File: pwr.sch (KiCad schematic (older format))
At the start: 60 parts, among them U1 FT601, U10 MIC94310, U11 PAM2305, U4 ECP5, U6 PAM2305, U7 NCP186, U8 MIC94310, U9 MIC94310, X2 CONN_01X08

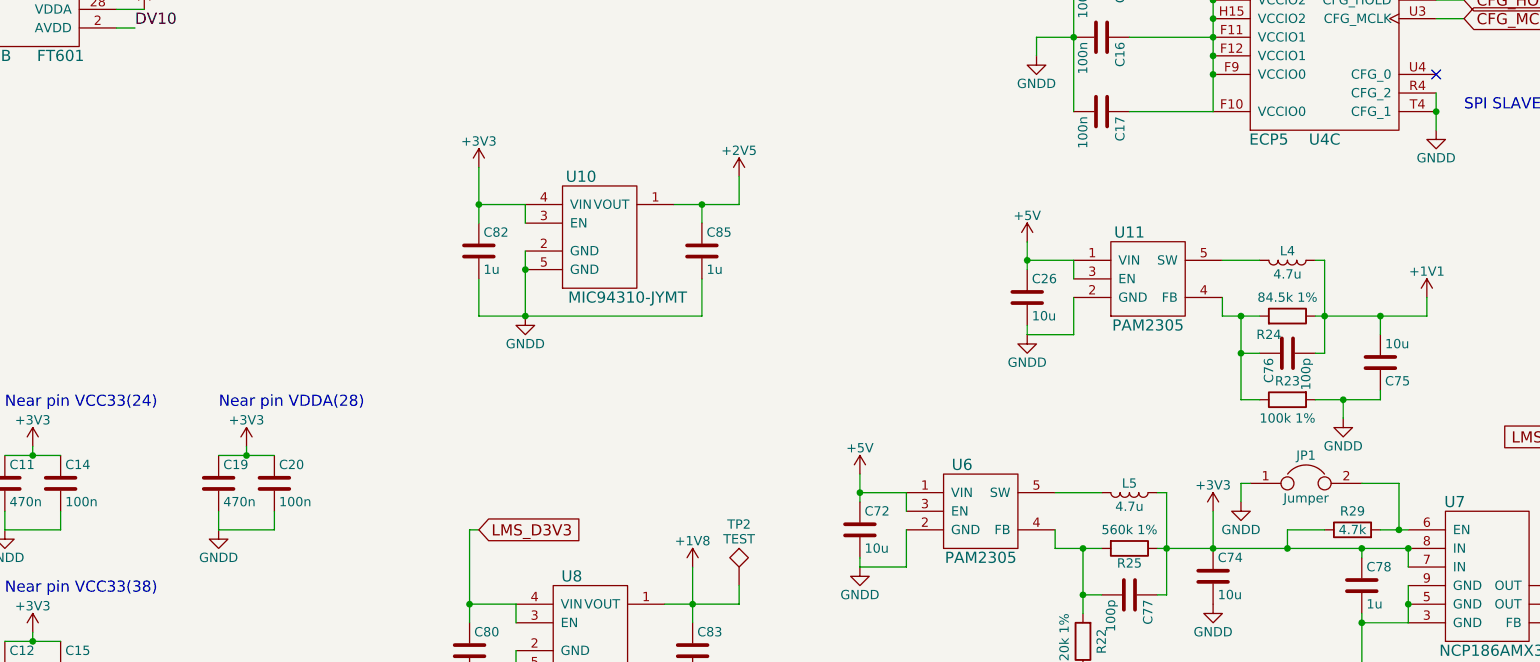
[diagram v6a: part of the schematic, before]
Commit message: Add leds. Traced LMS_3V3A LDO.
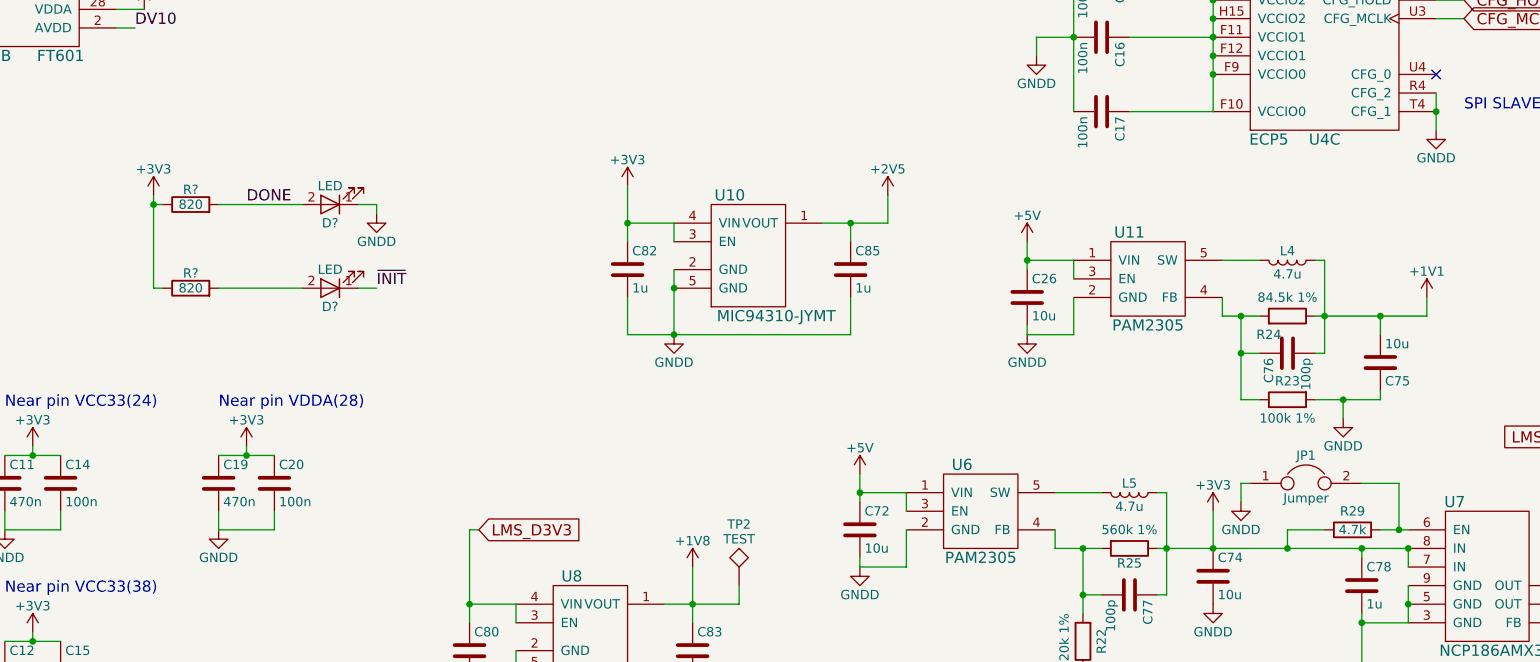
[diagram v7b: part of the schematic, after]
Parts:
- added D? (x2): LED, symbol LED
- added R? (x2): 820, symbol R
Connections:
- net +3V3: now also R?.1, R?.1
- net DONE: now also D?.2 (A), R?.2
- net GNDD: now also D?.1 (K)
- net ~INIT: now also D?.1 (K)
- new net: D?.2 (A), R?.2
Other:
- moved on the sheet: C82, C85, U10
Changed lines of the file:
@@
 	3950 7100 3950 7450
 $Comp
-L GNDD #PWR026
+L GNDD #PWR025
 U 1 1 58A7B03F
 P 3950 7450
-F 0 "#PWR026" H 3950 7200 50  0001 C CNN
+F 0 "#PWR025" H 3950 7200 50  0001 C CNN
 F 1 "GNDD" H 3950 7300 50  0000 C CNN
 F 2 "" H 3950 7450 50  0000 C CNN
@@
 Connection ~ 3950 7450
 $Comp
-L +1V8 #PWR027
+L +1V8 #PWR026
 U 1 1 58A7B123
 P 5850 5300
-F 0 "#PWR027" H 5850 5150 50  0001 C CNN
+F 0 "#PWR026" H 5850 5150 50  0001 C CNN
 F 1 "+1V8" H 5850 5440 50  0000 C CNN
 F 2 "" H 5850 5300 50  0000 C CNN
@@
 L MIC94310 U10
 U 1 1 58A7CAA3
-P 5150 3800
-F 0 "U10" H 5250 4400 60  0000 C CNN
-F 1 "MIC94310" H 5350 3750 60  0001 C CNN
-F 2 "sdr-foots:DFN-4" H 4600 3650 60  0001 C CNN
-F 3 "" H 4600 3650 60  0001 C CNN
-F 4 "MIC94310-JYMT" H 5500 3750 60  0000 C CNN "Part"
-	1    5150 3800
+P 5950 3900
+F 0 "U10" H 6050 4500 60  0000 C CNN
+F 1 "MIC94310" H 6150 3850 60  0001 C CNN
+F 2 "sdr-foots:DFN-4" H 5400 3750 60  0001 C CNN
+F 3 "" H 5400 3750 60  0001 C CNN
+F 4 "MIC94310-JYMT" H 6300 3850 60  0000 C CNN "Part"
+	1    5950 3900
 	1    0    0    -1
 $EndComp
@@
 L C C85
 U 1 1 58A7CAA9
-P 5900 3600
-F 0 "C85" H 5925 3700 50  0000 L CNN
-F 1 "1u" H 5925 3500 50  0000 L CNN
-F 2 "Capacitors_SMD:C_0603" H 5938 3450 50  0001 C CNN
-F 3 "" H 5900 3600 50  0000 C CNN
-	1    5900 3600
-	1    0    0    -1
-$EndComp
-Wire Wire Line
-	4950 3450 4950 3350
-Wire Wire Line
-	4950 3600 4950 3950
-$Comp
-L GNDD #PWR028
+P 6700 3700
+F 0 "C85" H 6725 3800 50  0000 L CNN
+F 1 "1u" H 6725 3600 50  0000 L CNN
+F 2 "Capacitors_SMD:C_0603" H 6738 3550 50  0001 C CNN
+F 3 "" H 6700 3700 50  0000 C CNN
+	1    6700 3700
+	1    0    0    -1
+$EndComp
+Wire Wire Line
+	5750 3550 5750 3450
+Wire Wire Line
+	5750 3700 5750 4050
+$Comp
+L GNDD #PWR027
 U 1 1 58A7CAB1
-P 4950 3950
-F 0 "#PWR028" H 4950 3700 50  0001 C CNN
-F 1 "GNDD" H 4950 3800 50  0000 C CNN
-F 2 "" H 4950 3950 50  0000 C CNN
-F 3 "" H 4950 3950 50  0000 C CNN
-	1    4950 3950
-	1    0    0    -1
-$EndComp
-Connection ~ 4950 3700
-Wire Wire Line
-	5900 3950 5900 3750
-Wire Wire Line
-	4700 3950 5900 3950
-Wire Wire Line
-	5900 3450 5900 3350
-Wire Wire Line
-	5750 3350 6100 3350
+P 5750 4050
+F 0 "#PWR027" H 5750 3800 50  0001 C CNN
+F 1 "GNDD" H 5750 3900 50  0000 C CNN
+F 2 "" H 5750 4050 50  0000 C CNN
+F 3 "" H 5750 4050 50  0000 C CNN
+	1    5750 4050
+	1    0    0    -1
+$EndComp
+Connection ~ 5750 3800
+Wire Wire Line
+	6700 4050 6700 3850
+Wire Wire Line
+	5500 4050 6700 4050
+Wire Wire Line
+	6700 3550 6700 3450
+Wire Wire Line
+	6550 3450 6900 3450
 $Comp
 L C C82
 U 1 1 58A7CABC
-P 4700 3600
-F 0 "C82" H 4725 3700 50  0000 L CNN
-F 1 "1u" H 4725 3500 50  0000 L CNN
-F 2 "Capacitors_SMD:C_0603" H 4738 3450 50  0001 C CNN
-F 3 "" H 4700 3600 50  0000 C CNN
-	1    4700 3600
-	1    0    0    -1
-$EndComp
-Wire Wire Line
-	4700 3150 4700 3450
-Wire Wire Line
-	4950 3350 4700 3350
-Wire Wire Line
-	4700 3750 4700 3950
-Connection ~ 4950 3950
-$Comp
-L +3V3 #PWR029
+P 5500 3700
+F 0 "C82" H 5525 3800 50  0000 L CNN
+F 1 "1u" H 5525 3600 50  0000 L CNN
+F 2 "Capacitors_SMD:C_0603" H 5538 3550 50  0001 C CNN
+F 3 "" H 5500 3700 50  0000 C CNN
+	1    5500 3700
+	1    0    0    -1
+$EndComp
+Wire Wire Line
+	5500 3250 5500 3550
+Wire Wire Line
+	5750 3450 5500 3450
+Wire Wire Line
+	5500 3850 5500 4050
+Connection ~ 5750 4050
+$Comp
+L +3V3 #PWR028
 U 1 1 58A7CAC6
-P 4700 3150
-F 0 "#PWR029" H 4700 3000 50  0001 C CNN
-F 1 "+3V3" H 4700 3290 50  0000 C CNN
-F 2 "" H 4700 3150 50  0000 C CNN
-F 3 "" H 4700 3150 50  0000 C CNN
-	1    4700 3150
-	1    0    0    -1
-$EndComp
-Connection ~ 4700 3350
-Connection ~ 5900 3350
+P 5500 3250
+F 0 "#PWR028" H 5500 3100 50  0001 C CNN
+F 1 "+3V3" H 5500 3390 50  0000 C CNN
+F 2 "" H 5500 3250 50  0000 C CNN
+F 3 "" H 5500 3250 50  0000 C CNN
+	1    5500 3250
+	1    0    0    -1
+$EndComp
+Connection ~ 5500 3450
+Connection ~ 6700 3450
 Wire Wire Line
 	9850 1500 9900 1500
@@
 Connection ~ 8650 1050
 $Comp
-L +3V3 #PWR030
+L +3V3 #PWR029
 U 1 1 58AD72E7
 P 8400 1250
-F 0 "#PWR030" H 8400 1100 50  0001 C CNN
+F 0 "#PWR029" H 8400 1100 50  0001 C CNN
 F 1 "+3V3" H 8400 1390 50  0000 C CNN
 F 2 "" H 8400 1250 50  0000 C CNN
@@
 Connection ~ 7900 1250
 $Comp
-L GNDD #PWR031
+L GNDD #PWR030
 U 1 1 58AD91E3
 P 7700 2550
-F 0 "#PWR031" H 7700 2300 50  0001 C CNN
+F 0 "#PWR030" H 7700 2300 50  0001 C CNN
 F 1 "GNDD" H 7700 2400 50  0000 C CNN
 F 2 "" H 7700 2550 50  0000 C CNN
@@
 $EndComp
 $Comp
-L +3V3 #PWR032
+L +3V3 #PWR031
 U 1 1 58AEBAC7
 P 6400 950
-F 0 "#PWR032" H 6400 800 50  0001 C CNN
+F 0 "#PWR031" H 6400 800 50  0001 C CNN
 F 1 "+3V3" H 6400 1090 50  0000 C CNN
 F 2 "" H 6400 950 50  0000 C CNN
@@
 $EndComp
 $Comp
-L GNDD #PWR033
+L GNDD #PWR032
 U 1 1 58B9309E
 P 7650 4050
-F 0 "#PWR033" H 7650 3800 50  0001 C CNN
+F 0 "#PWR032" H 7650 3800 50  0001 C CNN
 F 1 "GNDD" H 7650 3900 50  0000 C CNN
 F 2 "" H 7650 4050 50  0000 C CNN
@@
 	7650 4050 7650 4000
 $Comp
-L +5V #PWR034
+L +5V #PWR033
 U 1 1 58B930A5
 P 7650 3550
-F 0 "#PWR034" H 7650 3400 50  0001 C CNN
+F 0 "#PWR033" H 7650 3400 50  0001 C CNN
 F 1 "+5V" H 7650 3690 50  0000 C CNN
 F 2 "" H 7650 3550 50  0000 C CNN
@@
 Connection ~ 8650 1550
 $Comp
-L +2V5 #PWR035
+L +2V5 #PWR034
 U 1 1 58BCAEE2
-P 6100 3200
-F 0 "#PWR035" H 6100 3050 50  0001 C CNN
-F 1 "+2V5" H 6100 3340 50  0000 C CNN
-F 2 "" H 6100 3200 50  0000 C CNN
-F 3 "" H 6100 3200 50  0000 C CNN
-	1    6100 3200
-	1    0    0    -1
-$EndComp
-Wire Wire Line
-	6100 3350 6100 3200
+P 6900 3300
+F 0 "#PWR034" H 6900 3150 50  0001 C CNN
+F 1 "+2V5" H 6900 3440 50  0000 C CNN
+F 2 "" H 6900 3300 50  0000 C CNN
+F 3 "" H 6900 3300 50  0000 C CNN
+	1    6900 3300
+	1    0    0    -1
+$EndComp
+Wire Wire Line
+	6900 3450 6900 3300
 $Comp
 L Ferrite_Bead L3
@@
 	8200 950  8650 950
 $Comp
-L GNDD #PWR036
+L GNDD #PWR035
 U 1 1 58D24E6E
 P 9450 5900
-F 0 "#PWR036" H 9450 5650 50  0001 C CNN
+F 0 "#PWR035" H 9450 5650 50  0001 C CNN
 F 1 "GNDD" H 9450 5750 50  0000 C CNN
 F 2 "" H 9450 5900 50  0000 C CNN
@@
 	6100 5500 6100 5400
 Wire Wire Line
-	9700 5100 9550 5100
+	9550 5100 9700 5100
 Wire Wire Line
 	9450 4850 9650 4850
@@
 Connection ~ 9650 5100
 $Comp
-L GNDD #PWR037
+L GNDD #PWR036
 U 1 1 5936655F
 P 8800 4950
-F 0 "#PWR037" H 8800 4700 50  0001 C CNN
+F 0 "#PWR036" H 8800 4700 50  0001 C CNN
 F 1 "GNDD" H 8800 4800 50  0000 C CNN
 F 2 "" H 8800 4950 50  0000 C CNN
@@
 Wire Wire Line
 	4650 5100 4700 5100
+$Comp
+L R R?
+U 1 1 593912E7
+P 3150 3350
+F 0 "R?" V 3230 3350 50  0000 C CNN
+F 1 "820" V 3150 3350 50  0000 C CNN
+F 2 "" V 3080 3350 50  0001 C CNN
+F 3 "" H 3150 3350 50  0001 C CNN
+	1    3150 3350
+	0    -1   -1   0
+$EndComp
+$Comp
+L R R?
+U 1 1 593913B6
+P 3150 3800
+F 0 "R?" V 3230 3800 50  0000 C CNN
+F 1 "820" V 3150 3800 50  0000 C CNN
+F 2 "" V 3080 3800 50  0001 C CNN
+F 3 "" H 3150 3800 50  0001 C CNN
+	1    3150 3800
+	0    -1   -1   0
+$EndComp
+$Comp
+L LED D?
+U 1 1 5939158A
+P 3900 3350
+F 0 "D?" H 3900 3450 50  0000 C CNN
+F 1 "LED" H 3900 3250 50  0000 C CNN
+F 2 "" H 3900 3350 50  0001 C CNN
+F 3 "" H 3900 3350 50  0001 C CNN
+	1    3900 3350
+	-1   0    0    1
+$EndComp
+$Comp
+L LED D?
+U 1 1 5939162D
+P 3900 3800
+F 0 "D?" H 3900 3900 50  0000 C CNN
+F 1 "LED" H 3900 3700 50  0000 C CNN
+F 2 "" H 3900 3800 50  0001 C CNN
+F 3 "" H 3900 3800 50  0001 C CNN
+	1    3900 3800
+	-1   0    0    1
+$EndComp
+$Comp
+L +3V3 #PWR?
+U 1 1 593919B2
+P 2950 3300
+F 0 "#PWR?" H 2950 3150 50  0001 C CNN
+F 1 "+3V3" H 2950 3440 50  0000 C CNN
+F 2 "" H 2950 3300 50  0000 C CNN
+F 3 "" H 2950 3300 50  0000 C CNN
+	1    2950 3300
+	1    0    0    -1
+$EndComp
+Wire Wire Line
+	3300 3350 3750 3350
+Wire Wire Line
+	2950 3350 3000 3350
+Wire Wire Line
+	2950 3800 3000 3800
+Wire Wire Line
+	2950 3300 2950 3800
+Connection ~ 2950 3350
+Wire Wire Line
+	3300 3800 3750 3800
+$Comp
+L GNDD #PWR?
+U 1 1 5939291E
+P 4150 3400
+F 0 "#PWR?" H 4150 3150 50  0001 C CNN
+F 1 "GNDD" H 4150 3250 50  0000 C CNN
+F 2 "" H 4150 3400 50  0000 C CNN
+F 3 "" H 4150 3400 50  0000 C CNN
+	1    4150 3400
+	1    0    0    -1
+$EndComp
+Text Label 3450 3350 0    60   ~ 0
+DONE
+Wire Wire Line
+	4150 3400 4150 3350
+Wire Wire Line
+	4150 3350 4050 3350
+Text Label 4150 3800 0    60   ~ 0
+~INIT
+Wire Wire Line
+	4150 3800 4050 3800
 $EndSCHEMATC

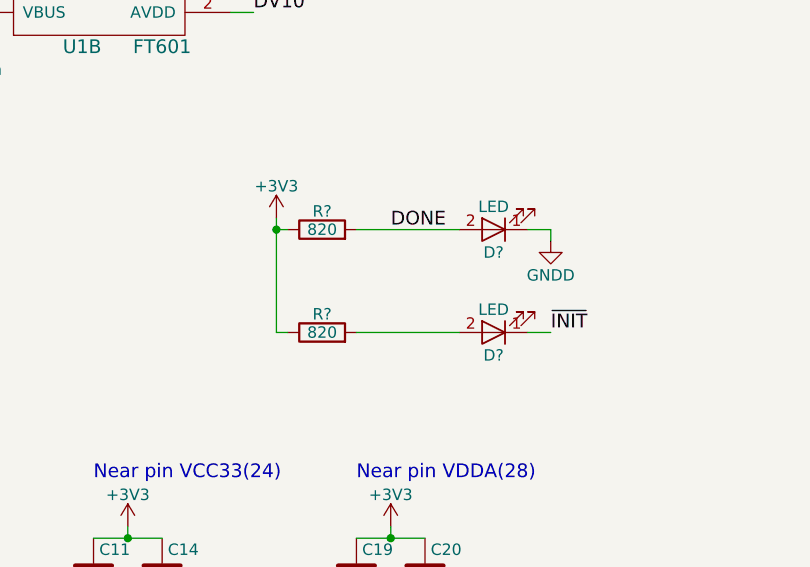
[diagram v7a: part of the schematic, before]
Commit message: Start tracing IO Fix connector for Rpi Use LED indicator for TX/RX LEDs
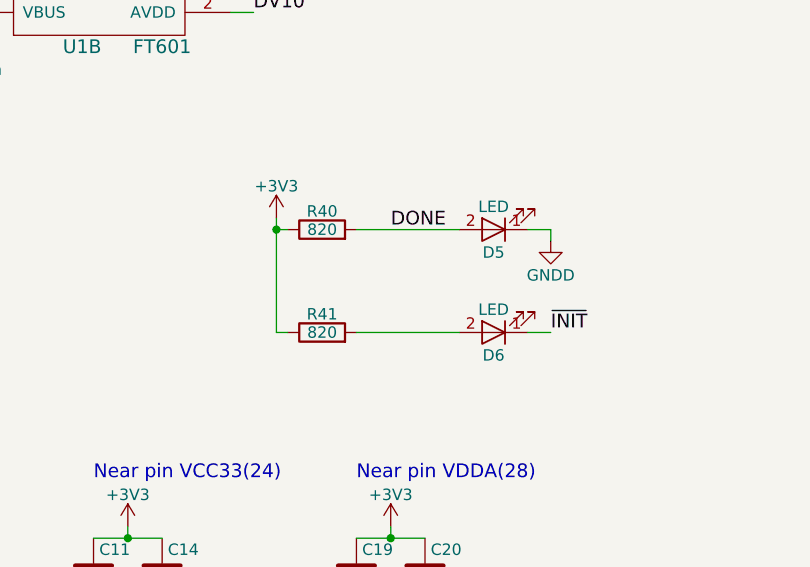
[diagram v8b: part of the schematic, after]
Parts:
- D5, D6: renamed from D?; footprint (none) -> LEDs:LED_0603
- R40, R41: renamed from R?; footprint (none) -> Resistors_SMD:R_0603
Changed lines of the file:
@@
 	4650 5100 4700 5100
 $Comp
-L R R?
+L R R40
 U 1 1 593912E7
 P 3150 3350
-F 0 "R?" V 3230 3350 50  0000 C CNN
+F 0 "R40" V 3230 3350 50  0000 C CNN
 F 1 "820" V 3150 3350 50  0000 C CNN
-F 2 "" V 3080 3350 50  0001 C CNN
+F 2 "Resistors_SMD:R_0603" V 3080 3350 50  0001 C CNN
 F 3 "" H 3150 3350 50  0001 C CNN
 	1    3150 3350
@@
 $EndComp
 $Comp
-L R R?
+L R R41
 U 1 1 593913B6
 P 3150 3800
-F 0 "R?" V 3230 3800 50  0000 C CNN
+F 0 "R41" V 3230 3800 50  0000 C CNN
 F 1 "820" V 3150 3800 50  0000 C CNN
-F 2 "" V 3080 3800 50  0001 C CNN
+F 2 "Resistors_SMD:R_0603" V 3080 3800 50  0001 C CNN
 F 3 "" H 3150 3800 50  0001 C CNN
 	1    3150 3800
@@
 $EndComp
 $Comp
-L LED D?
+L LED D5
 U 1 1 5939158A
 P 3900 3350
-F 0 "D?" H 3900 3450 50  0000 C CNN
+F 0 "D5" H 3900 3450 50  0000 C CNN
 F 1 "LED" H 3900 3250 50  0000 C CNN
-F 2 "" H 3900 3350 50  0001 C CNN
+F 2 "LEDs:LED_0603" H 3900 3350 50  0001 C CNN
 F 3 "" H 3900 3350 50  0001 C CNN
 	1    3900 3350
@@
 $EndComp
 $Comp
-L LED D?
+L LED D6
 U 1 1 5939162D
 P 3900 3800
-F 0 "D?" H 3900 3900 50  0000 C CNN
+F 0 "D6" H 3900 3900 50  0000 C CNN
 F 1 "LED" H 3900 3700 50  0000 C CNN
-F 2 "" H 3900 3800 50  0001 C CNN
+F 2 "LEDs:LED_0603" H 3900 3800 50  0001 C CNN
 F 3 "" H 3900 3800 50  0001 C CNN
 	1    3900 3800
@@
 $EndComp
 $Comp
-L +3V3 #PWR?
+L +3V3 #PWR037
 U 1 1 593919B2
 P 2950 3300
-F 0 "#PWR?" H 2950 3150 50  0001 C CNN
+F 0 "#PWR037" H 2950 3150 50  0001 C CNN
 F 1 "+3V3" H 2950 3440 50  0000 C CNN
 F 2 "" H 2950 3300 50  0000 C CNN
@@
 	3300 3800 3750 3800
 $Comp
-L GNDD #PWR?
+L GNDD #PWR038
 U 1 1 5939291E
 P 4150 3400
-F 0 "#PWR?" H 4150 3150 50  0001 C CNN
+F 0 "#PWR038" H 4150 3150 50  0001 C CNN
 F 1 "GNDD" H 4150 3250 50  0000 C CNN
 F 2 "" H 4150 3400 50  0000 C CNN
